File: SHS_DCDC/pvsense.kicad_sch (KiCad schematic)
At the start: 9 parts, among them U3 LMV324AIDR

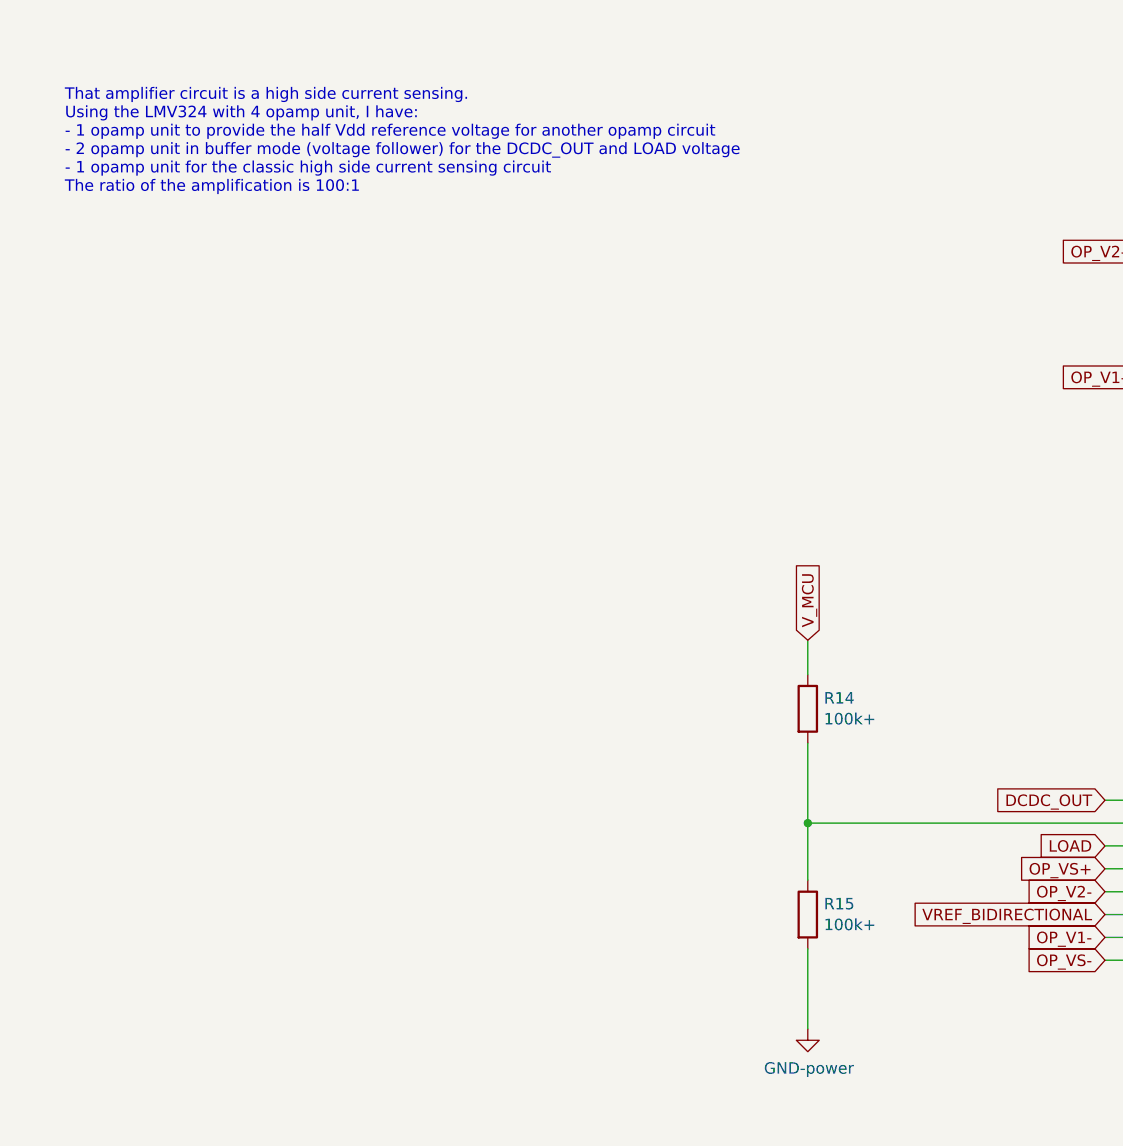
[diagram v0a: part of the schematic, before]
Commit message: PV & BAT V sense
Adding 2 same blocks allowing the measure by ADC of the PV and Battery voltage on demand through power gating technique
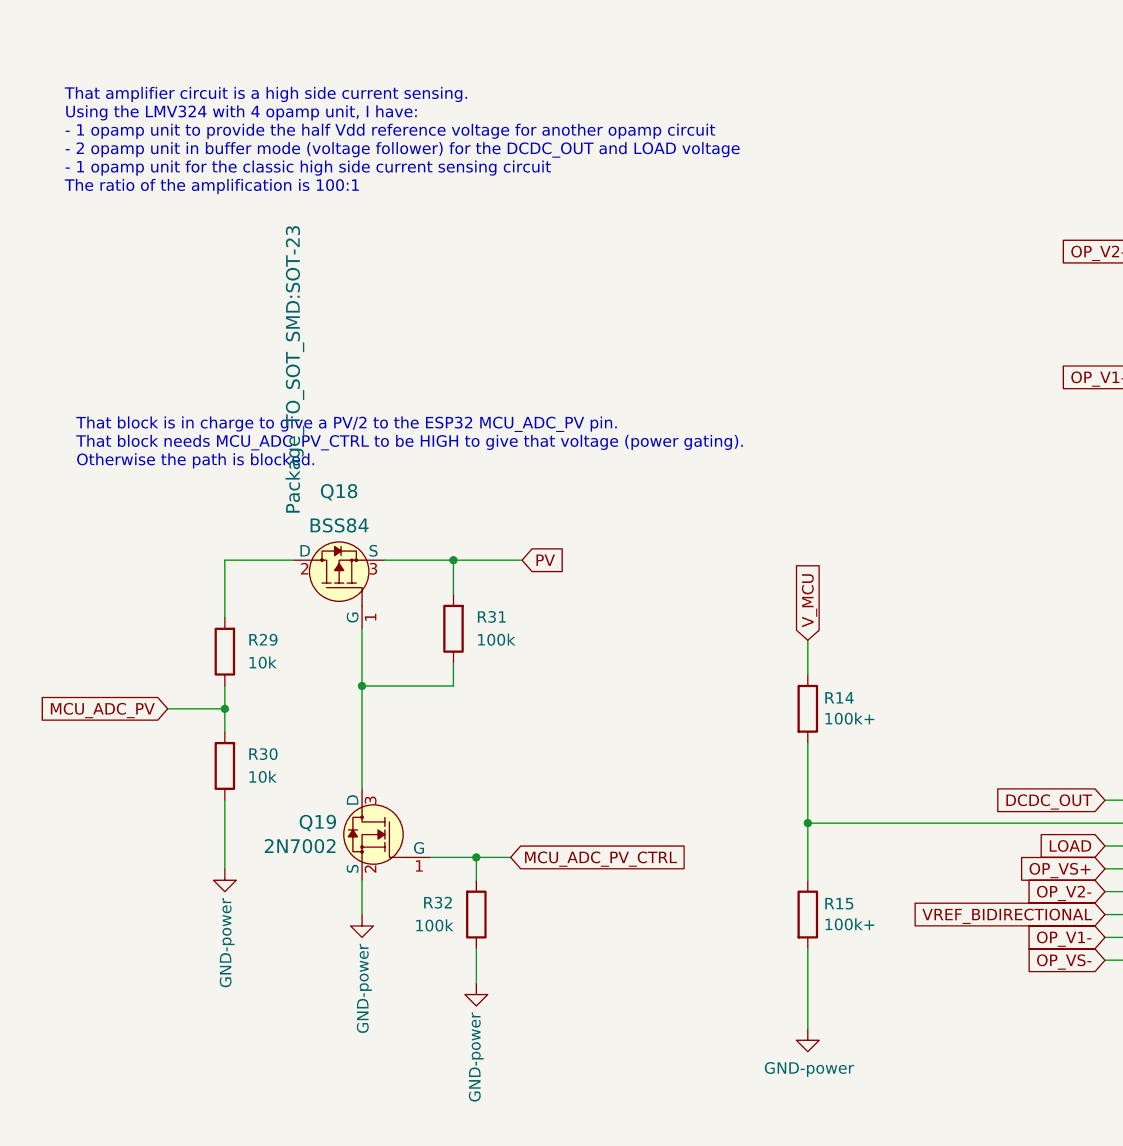
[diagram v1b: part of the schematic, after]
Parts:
- added Q18: BSS84, Package_TO_SOT_SMD:SOT-23, symbol dk_Transistors-FETs-MOSFETs-Single:BSS84
- added Q19: 2N7002, Package_TO_SOT_SMD:SOT-23, symbol SHS_DCDC:2N7002-dk_Transistors-FETs-MOSFETs-Single
- added R29, R30: 10k, Resistor_SMD:R_0402_1005Metric, symbol Device:R
- added R31, R32: 100k, Resistor_SMD:R_0402_1005Metric, symbol Device:R
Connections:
- net GND: now also Q19.2 (S), R30.1, R32.1
- new net: Q18.2 (D), R29.2
- new net: Q18.1 (G), Q19.3 (D), R31.1
- new net MCU_ADC_PV: R29.1, R30.2
- new net MCU_ADC_PV_CTRL: Q19.1 (G), R32.2
- new net PV: Q18.3 (S), R31.2
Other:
- note added: "That block is in charge to give a PV/2 to the ESP32 MCU_ADC_PV pin. That block needs MCU_ADC_PV_CTRL to be HIGH to give that voltage (power gating). Otherwise the path is blocked."

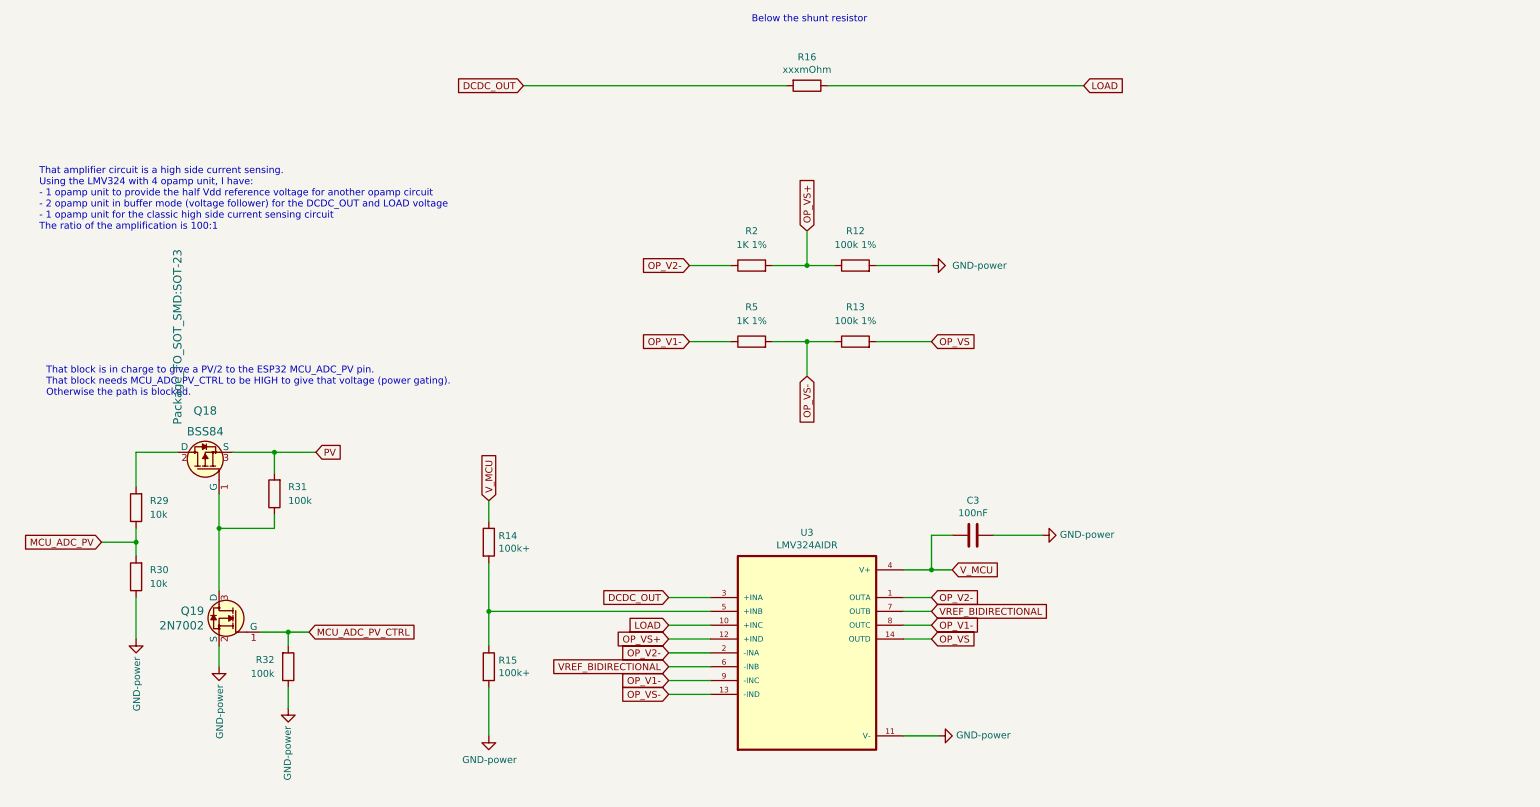
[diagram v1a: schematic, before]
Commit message: DFU update
PCB update to setup 3 ways of FW/Debug capability:
1. JTAG (FW & Debug)
2. USB DFU (FW & Debug)
3. UART (FW only)
With BOOT0 button installed too
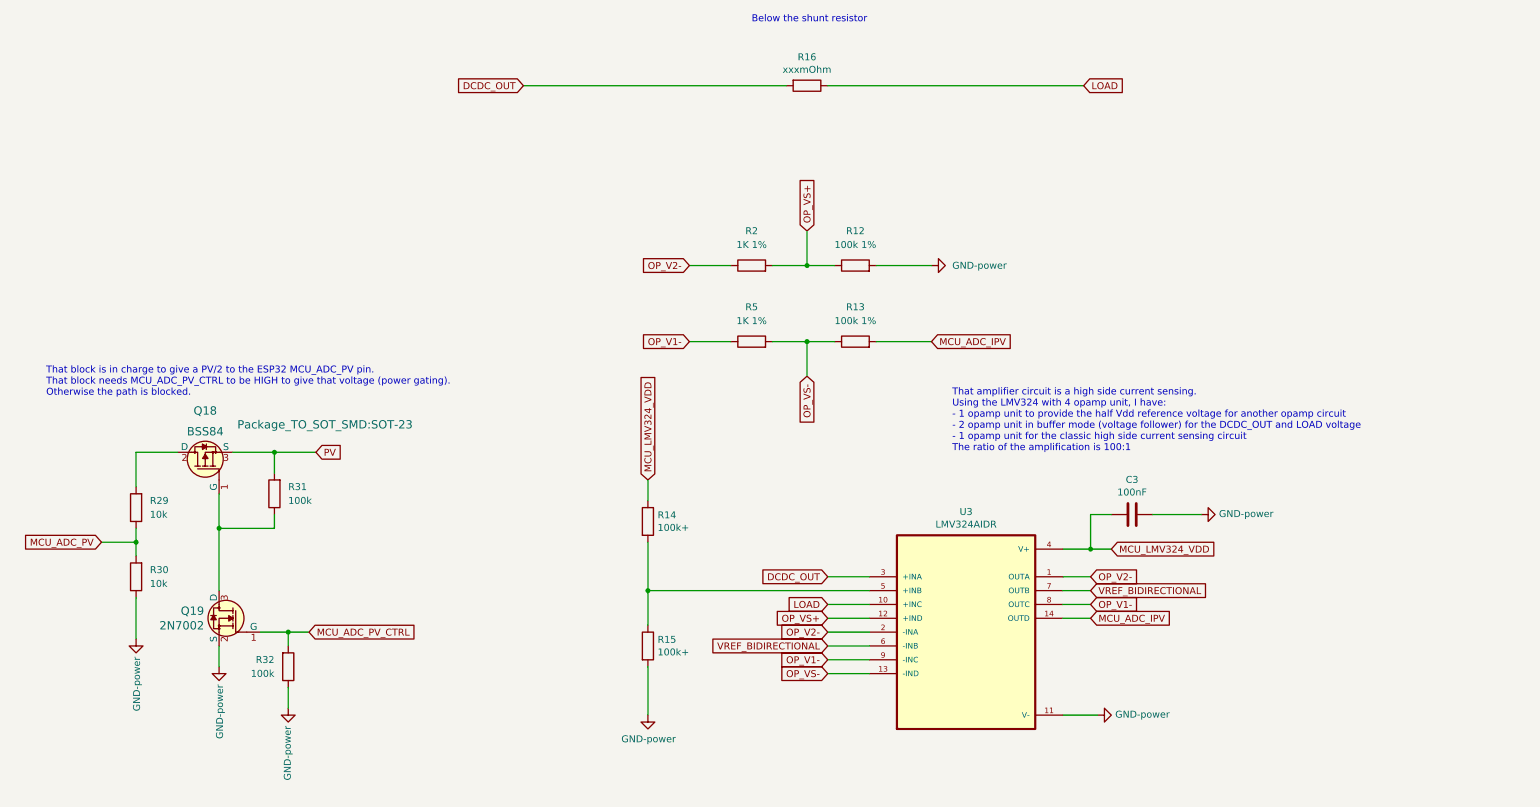
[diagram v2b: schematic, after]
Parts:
- C3: footprint Capacitor_SMD:C_0603_1608Metric -> Capacitor_SMD:C_0402_1005Metric
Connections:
- net OP_VS renamed MCU_ADC_IPV
- net V_MCU renamed MCU_LMV324_VDD
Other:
- moved on the sheet: C3, R14, R15, U3

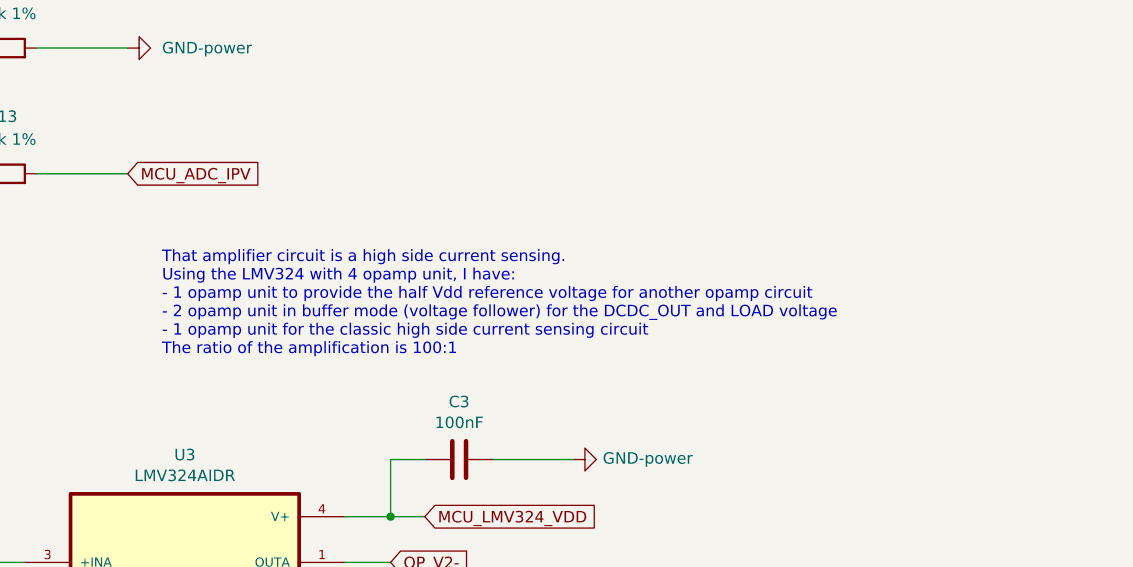
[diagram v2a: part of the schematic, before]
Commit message: PV input Power
Big modification on the PV input power protection, precisely on the reverse battery current protection, and also on the switch between direct PV charging and the DCDC converter
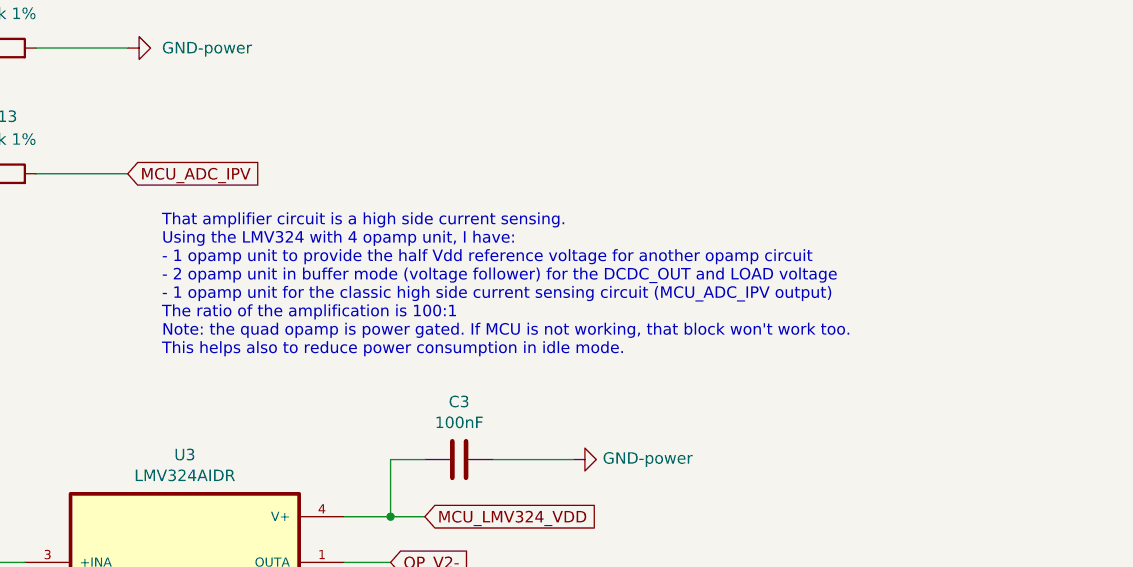
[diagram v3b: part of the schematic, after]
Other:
- note added: "That amplifier circuit is a high side current sensing. Using the LMV324 with 4 opamp unit, I have: - 1 opamp unit to provide the half Vdd reference voltage for another opamp circuit - 2 opamp unit in buffer mode (voltage follower) for the DCDC_OUT and LOAD voltage - 1 opamp unit for the classic high side current sensing circuit (MCU_ADC_IPV output) The ratio of the amplification is 100:1 Note: th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"
- note removed: "That amplifier circuit is a high side current sensing. Using the LMV324 with 4 opamp unit, I have: - 1 opamp unit to provide the half Vdd reference voltage for another opamp circuit - 2 opamp unit in buffer mode (voltage follower) for the DCDC_OUT and LOAD voltage - 1 opamp unit for the classic high side current sensing circuit The ratio of the amplification is 100:1"
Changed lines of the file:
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@@
     (stroke (width 0) (type default) (color 0 0 0 0))
   )
-  (text "That amplifier circuit is a high side current sensing.\nUsing the LMV324 with 4 opamp unit, I have:\n- 1 opamp unit to provide the half Vdd reference voltage for another opamp circuit\n- 2 opamp unit in buffer mode (voltage follower) for the DCDC_OUT and LOAD voltage\n- 1 opamp unit for the classic high side current sensing circuit\nThe ratio of the amplification is 100:1"
+  (text "That amplifier circuit is a high side current sensing.\nUsing the LMV324 with 4 opamp unit, I have:\n- 1 opamp unit to provide the half Vdd reference voltage for another opamp circuit\n- 2 opamp unit in buffer mode (voltage follower) for the DCDC_OUT and LOAD voltage\n- 1 opamp unit for the classic high side current sensing circuit (MCU_ADC_IPV output)\nThe ratio of the amplification is 100:1\nNote: the quad opamp is power gated. If MCU is not working, that block won't work too.\nThis helps also to reduce power consumption in idle mode."
     (at 184.15 96.52 0)
     (effects (font (size 1.27 1.27)) (justify left bottom))

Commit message: Final_check stage
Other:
- note added: "Below the shunt resistor measuring the current coming from the PV"
- note removed: "Below the shunt resistor"
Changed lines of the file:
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@@
     (effects (font (size 1.27 1.27)) (justify left bottom))
   )
-  (text "Below the shunt resistor\n" (at 147.32 17.78 0)
+  (text "Below the shunt resistor measuring the current coming from the PV\n"
+    (at 115.57 20.32 0)
     (effects (font (size 1.27 1.27)) (justify left bottom))
   )
